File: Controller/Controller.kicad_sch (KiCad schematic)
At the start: 40 parts, among them SW2 SW_Push, SW3 SW_Push, SW4 SW_Push, SW5 SW_Push, SW6 SW_Push, SW7 SW_Push, SW8 SW_Push, SW9 SW_Push

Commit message: Add sections
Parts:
- R1: value ??? -> 400
- renumbered ON/OFF-Switch to ON/OFF-Switch1
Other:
- moved on the sheet: C1, LED1, LED10, LED2, LED3, LED4, LED5, LED6, LED7, LED8, LED9, Level-Shifter-1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

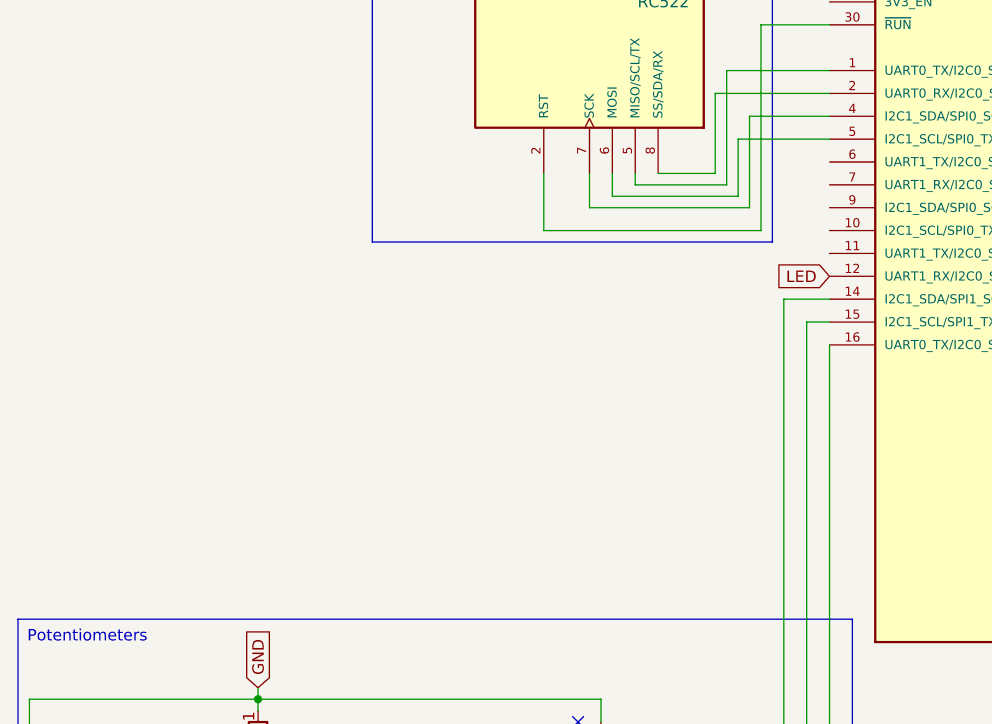
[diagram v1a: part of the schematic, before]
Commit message: Edit symbols and add screen to schematic
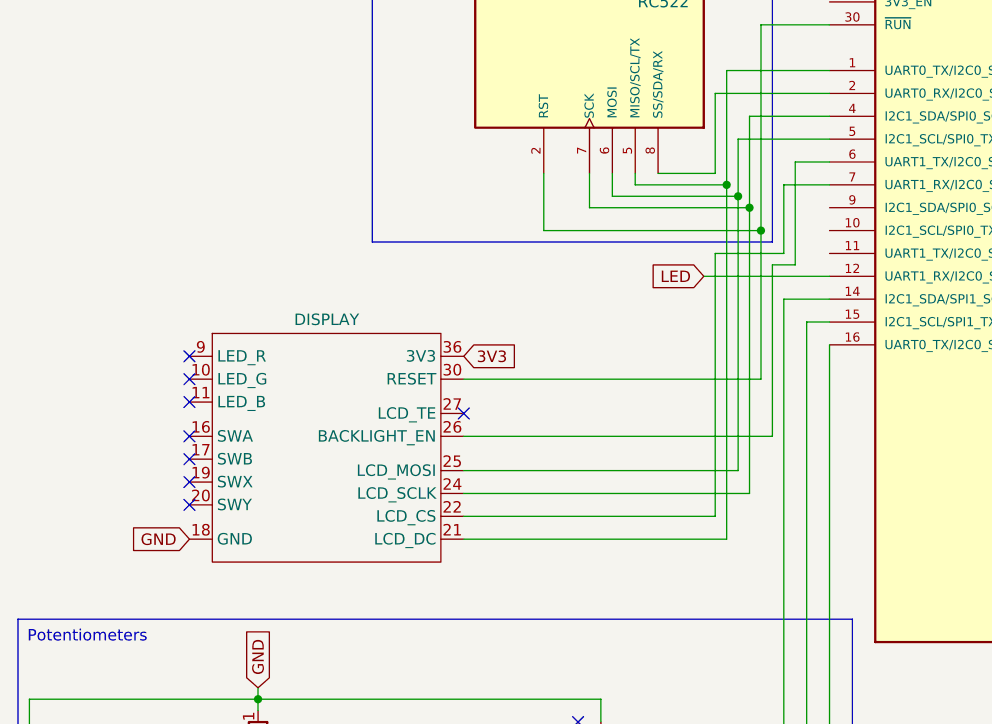
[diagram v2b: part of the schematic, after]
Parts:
- added DISPLAY: ~, symbol PIM580:PIM580
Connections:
- net 3V3: now also DISPLAY.36 (3V3)
- net GND: now also DISPLAY.18 (GND)
- net at NFC-1.5 (MISO/SCL/TX), PICO-1.1 (UART0_TX/I2C0_SDA/SPI0_RX/GP0): now also DISPLAY.21 (LCD_DC)
- net at NFC-1.2 (RST), PICO-1.30 (~{RUN}): now also DISPLAY.30 (RESET)
- net at NFC-1.7 (SCK), PICO-1.4 (I2C1_SDA/SPI0_SCK/GP2): now also DISPLAY.24 (LCD_SCLK)
- net at NFC-1.6 (MOSI), PICO-1.5 (I2C1_SCL/SPI0_TX/GP3): now also DISPLAY.25 (LCD_MOSI)
- net at PICO-1.6 (UART1_TX/I2C0_SDA/SPI0_RX/GP4): now also DISPLAY.26 (BACKLIGHT_EN)
- net at PICO-1.7 (UART1_RX/I2C0_SCL/SPI0_CSN/GP5): now also DISPLAY.22 (LCD_CS)
- no-connect marks 19 -> 27

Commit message: Add mosfet definition
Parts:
- MOS-P1: value ??? -> DMG2305UX-7
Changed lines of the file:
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@@
 		(dnp no)
 		(property "Reference" "MOS-P1"
-			(at 276.352 46.482 90)
+			(at 275.844 50.292 90)
 			(effects
 				(font
@@
 			)
 		)
-		(property "Value" "???"
-			(at 276.352 49.022 90)
+		(property "Value" "DMG2305UX-7"
+			(at 275.844 52.832 90)
 			(effects
 				(font

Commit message: Update
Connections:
- net GP22: now reaches PICO-1.29 (GP22)
- net GP22: now also NFC-1.2 (RST)
- net at DISPLAY.30 (RESET), PICO-1.30 (~{RUN}): no longer NFC-1.2 (RST)
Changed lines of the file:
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@@
-	)
-	(junction
-		(at 95.25 100.33)
-		(diameter 0)
-		(color 0 0 0 0)
 	)
 	(junction
@@
 	(wire
 		(pts
-			(xy 71.12 100.33) (xy 71.12 93.98)
-		)
-		(stroke
-			(width 0)
-			(type default)
-		)
-	)
-	(wire
-		(pts
 			(xy 93.98 87.63) (xy 93.98 97.79)
 		)
@@
 	(wire
 		(pts
-			(xy 95.25 100.33) (xy 95.25 116.84)
+			(xy 95.25 77.47) (xy 95.25 116.84)
 		)
 		(stroke
@@
 	(wire
 		(pts
-			(xy 95.25 77.47) (xy 95.25 100.33)
-		)
-		(stroke
-			(width 0)
-			(type default)
-		)
-	)
-	(wire
-		(pts
 			(xy 76.2 97.79) (xy 76.2 93.98)
 		)
@@
 			(type default)
 			(color 255 0 0 1)
-		)
-	)
-	(wire
-		(pts
-			(xy 95.25 100.33) (xy 71.12 100.33)
-		)
-		(stroke
-			(width 0)
-			(type default)
 		)
 	)
@@
 			)
 			(justify left top)
+		)
+	)
+	(global_label "GP22"
+		(shape input)
+		(at 199.39 105.41 0)
+		(fields_autoplaced yes)
+		(effects
+			(font
+				(size 1.27 1.27)
+			)
+			(justify left)
+		)
+		(property "Intersheetrefs" "${INTERSHEET_REFS}"
+			(at 207.3342 105.41 0)
+			(effects
+				(font
+					(size 1.27 1.27)
+				)
+				(justify left)
+				(hide yes)
+			)
 		)
 	)
@@
 			(effects
 				(font
+					(size 1.27 1.27)
+				)
+				(justify right)
+				(hide yes)
+			)
+		)
+	)
+	(global_label "GP22"
+		(shape input)
+		(at 71.12 93.98 270)
+		(fields_autoplaced yes)
+		(effects
+			(font
+				(size 1.27 1.27)
+			)
+			(justify right)
+		)
+		(property "Intersheetrefs" "${INTERSHEET_REFS}"
+			(at 71.12 101.9242 90)
+			(effects
+				(font

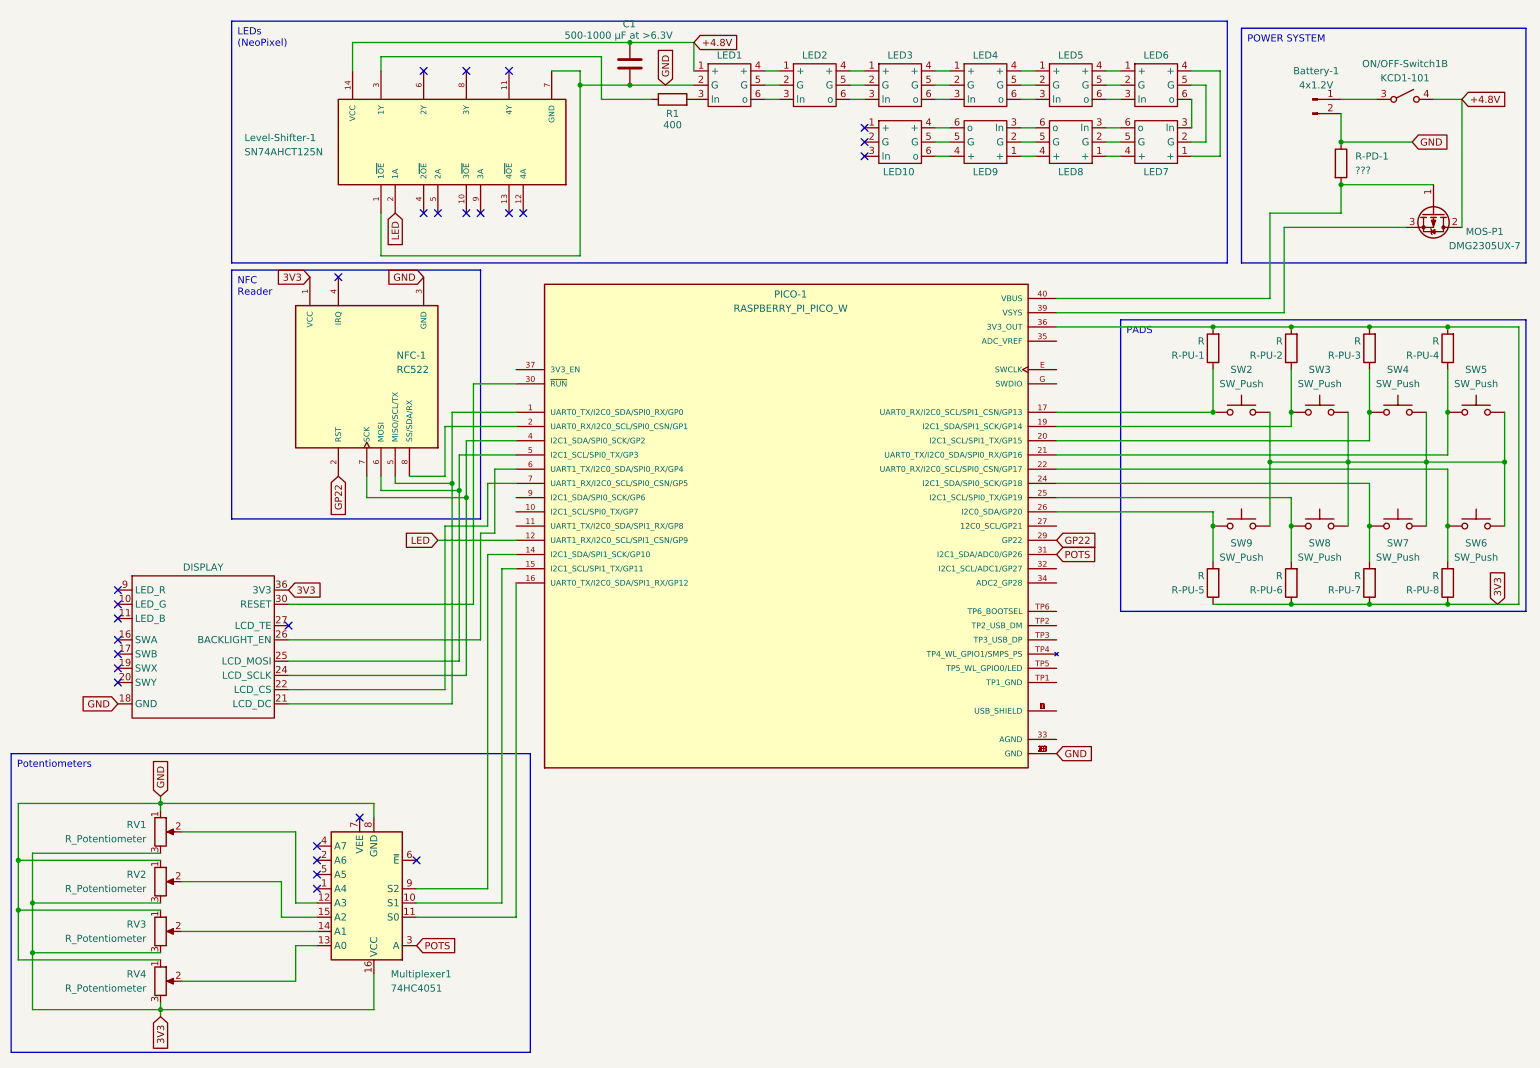
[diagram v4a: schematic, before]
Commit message: Rewire display
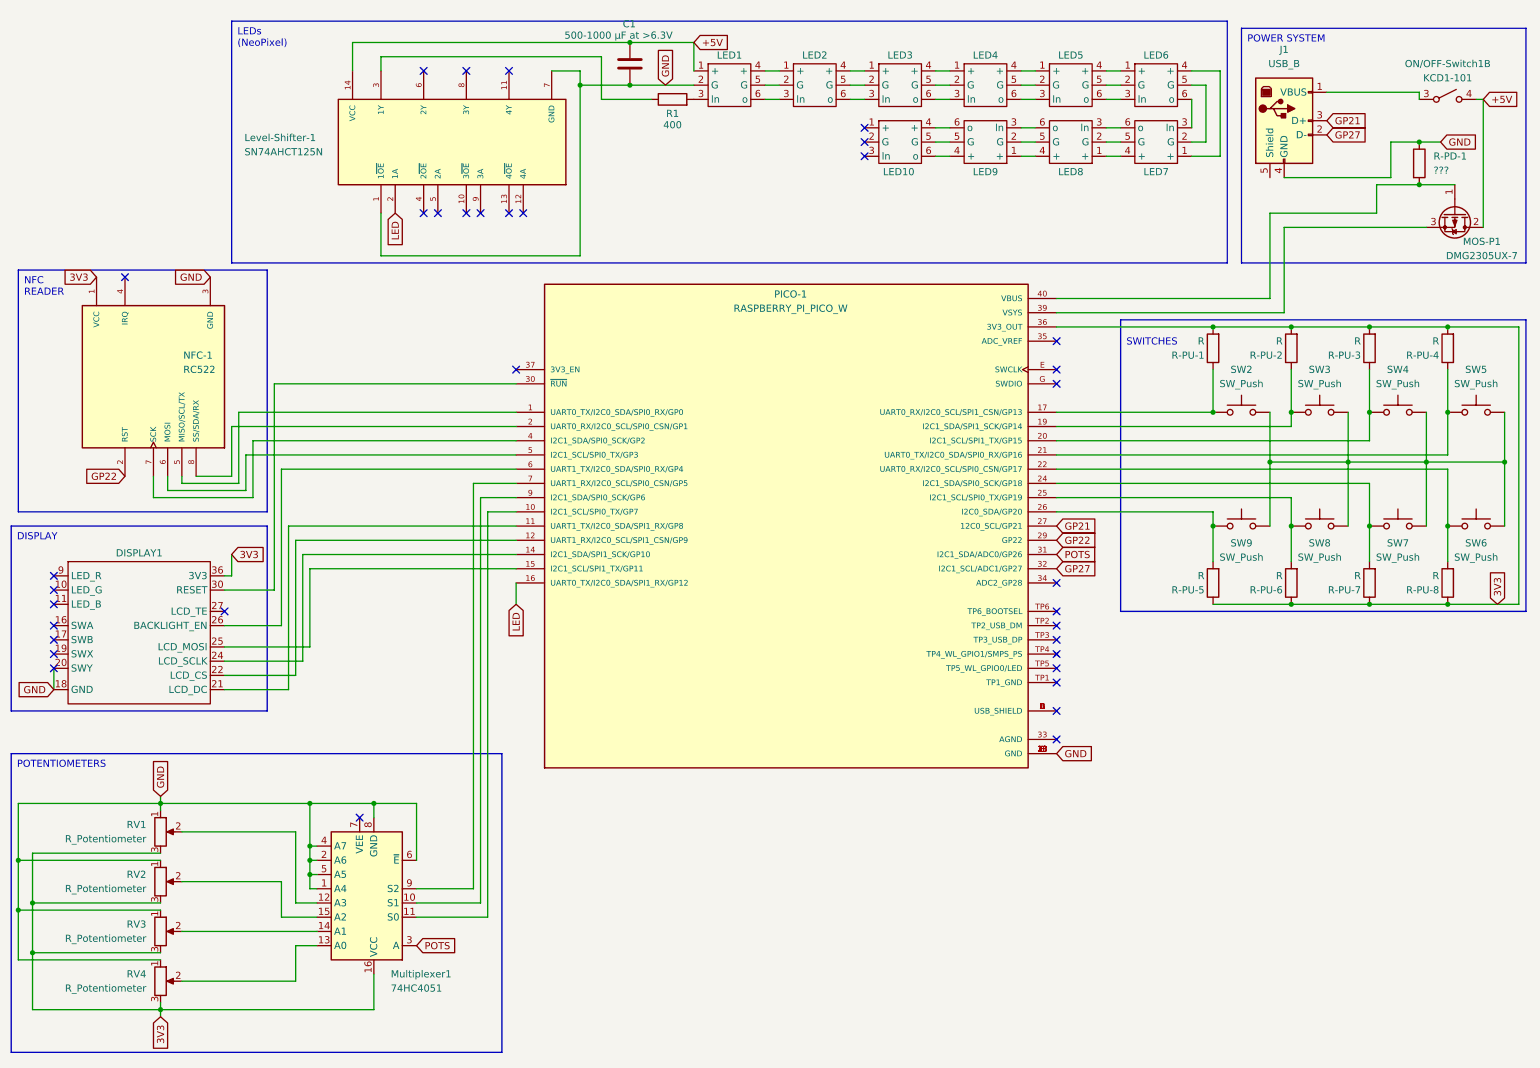
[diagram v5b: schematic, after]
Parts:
- removed Battery-1: 4x1.2V, Connector_PinHeader_1.00mm:PinHeader_1x02_P1.00mm_Vertical, symbol Connector:Conn_01x02_Pin
- added J1: USB_B, Connector_PinHeader_1.00mm:PinHeader_1x04_P1.00mm_Vertical, symbol Connector:USB_B
- DISPLAY1: renamed from DISPLAY; footprint (none) -> Connector_PinHeader_1.00mm:PinHeader_1x08_P1.00mm_Vertical
- MOS-P1: footprint Package_TO_SOT_THT:TO-220-3_Vertical -> (none)
- NFC-1: footprint CEG006900:MODULE_CEG006900 -> Connector_PinHeader_1.00mm:PinHeader_1x07_P1.00mm_Vertical
- R1: footprint (none) -> Resistor_THT:R_Axial_DIN0204_L3.6mm_D1.6mm_P5.08mm_Horizontal
- SW2, SW3, SW4, SW5, SW6, SW7, SW8, SW9: footprint Button_Switch_THT:SW_PUSH-12mm -> (none)
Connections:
- net GND: now also DISPLAY1.20 (SWY), Multiplexer1.1 (A4), Multiplexer1.2 (A6), Multiplexer1.4 (A7), Multiplexer1.5 (A5), Multiplexer1.6 (~{E}), J1.4 (GND)
- net LED: now also PICO-1.16 (UART0_TX/I2C0_SDA/SPI1_RX/GP12); no longer PICO-1.12 (UART1_RX/I2C0_SCL/SPI1_CSN/GP9)
- net at NFC-1.5 (MISO/SCL/TX), PICO-1.1 (UART0_TX/I2C0_SDA/SPI0_RX/GP0): no longer DISPLAY1.21 (LCD_DC)
- net at PICO-1.10 (I2C1_SCL/SPI0_TX/GP7): now also Multiplexer1.11 (S0)
- net at PICO-1.11 (UART1_TX/I2C0_SDA/SPI1_RX/GP8): now also DISPLAY1.21 (LCD_DC)
- net at PICO-1.14 (I2C1_SDA/SPI1_SCK/GP10): now also DISPLAY1.24 (LCD_SCLK); no longer Multiplexer1.9 (S2)
- net at PICO-1.15 (I2C1_SCL/SPI1_TX/GP11): now also DISPLAY1.25 (LCD_MOSI); no longer Multiplexer1.10 (S1)
- net GP21: now reaches PICO-1.27 (12C0_SCL/GP21)
- net GP21: now also J1.3 (D+)
- net GP27: now reaches PICO-1.32 (I2C1_SCL/ADC1/GP27)
- net GP27: now also J1.2 (D-)
- net at NFC-1.7 (SCK), PICO-1.4 (I2C1_SDA/SPI0_SCK/GP2): no longer DISPLAY1.24 (LCD_SCLK)
- net at NFC-1.6 (MOSI), PICO-1.5 (I2C1_SCL/SPI0_TX/GP3): no longer DISPLAY1.25 (LCD_MOSI)
- net at DISPLAY1.22 (LCD_CS): now also PICO-1.12 (UART1_RX/I2C0_SCL/SPI1_CSN/GP9); no longer PICO-1.7 (UART1_RX/I2C0_SCL/SPI0_CSN/GP5)
- net at PICO-1.9 (I2C1_SDA/SPI0_SCK/GP6): now also Multiplexer1.10 (S1)
- net at ON/OFF-Switch1.3 (A): now also J1.1 (VBUS)
- net +4.8V renamed +5V
- new net: Multiplexer1.9 (S2), PICO-1.7 (UART1_RX/I2C0_SCL/SPI0_CSN/GP5)
- no-connect marks 27 -> 35
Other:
- moved on the sheet: DISPLAY1, MOS-P1, NFC-1, ON/OFF-Switch1B, R-PD-1

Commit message: Add components and lign up PCB
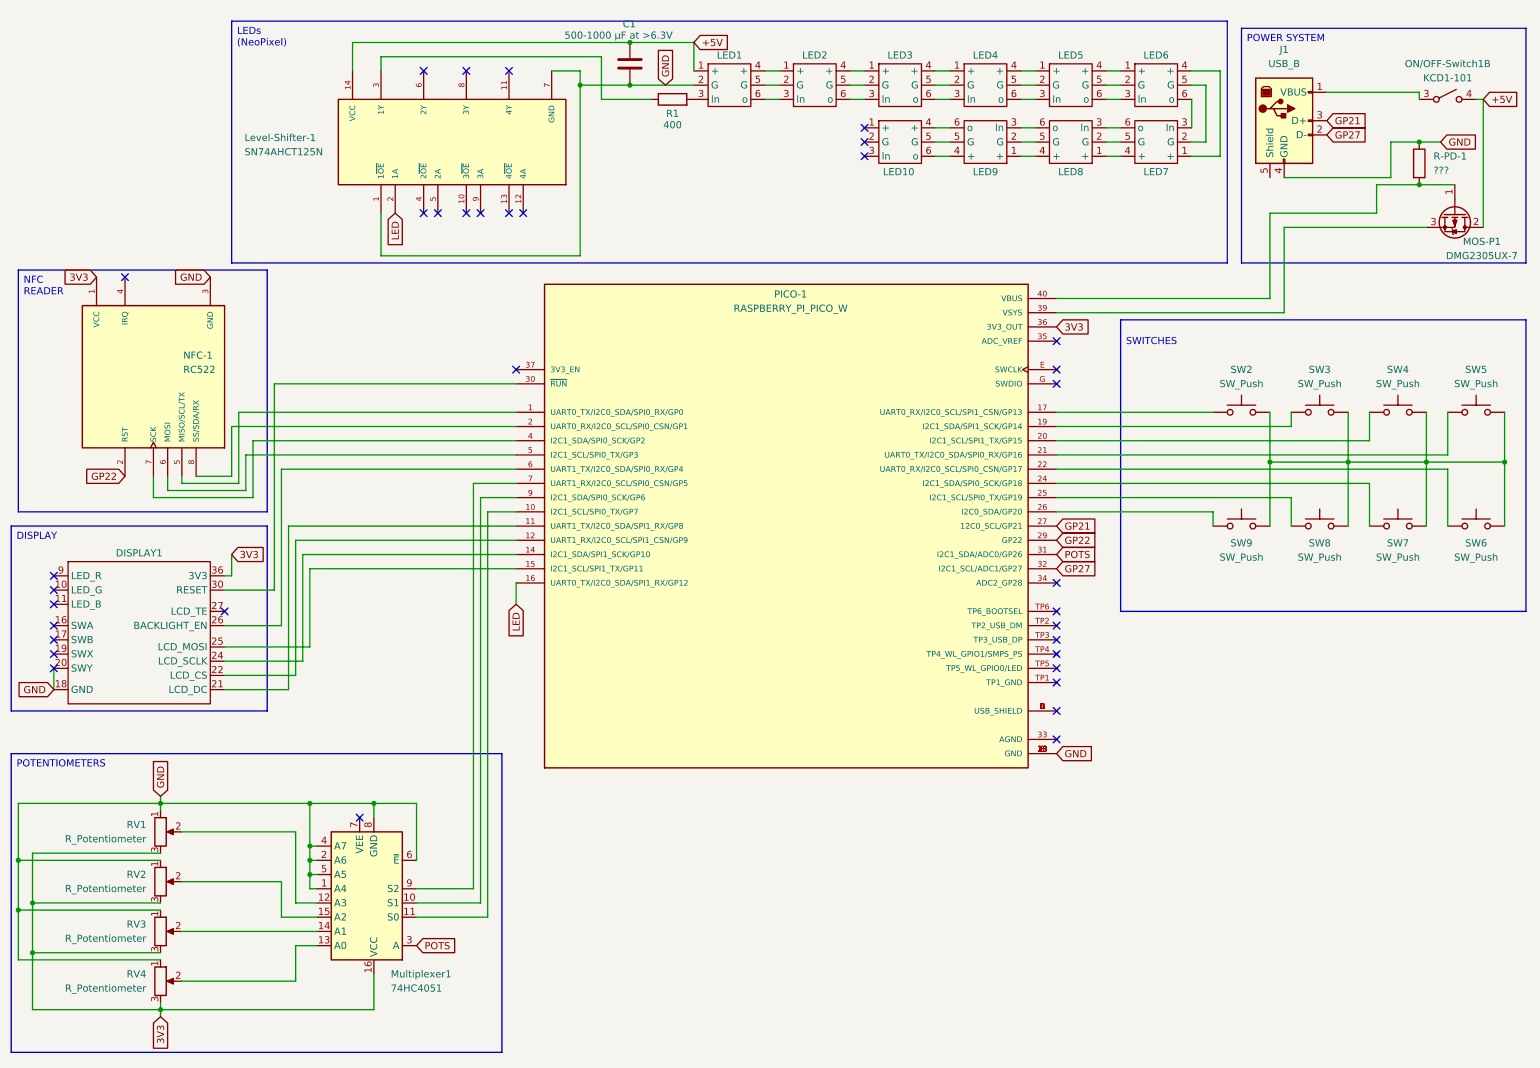
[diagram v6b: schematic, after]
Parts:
- removed R-PU-1, R-PU-2, R-PU-3, R-PU-4, R-PU-5, R-PU-6, R-PU-7, R-PU-8: R, Resistor_THT:R_Axial_DIN0204_L3.6mm_D1.6mm_P5.08mm_Horizontal, symbol Device:R
- DISPLAY1: footprint Connector_PinHeader_1.00mm:PinHeader_1x08_P1.00mm_Vertical -> PIM580:display-footprint
- PICO-1: footprint RASPBERRY_PI_PICO_W:MODULE_RASPBERRY_PI_PICO_W -> RASPBERRY_PI_PICO_W:pico-footprint
- SW2, SW3, SW4, SW5, SW6, SW7, SW8, SW9: footprint (none) -> Gateron:SW_Gateron_LowProfile_HotSwap_THT (1)

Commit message: PCB Routing
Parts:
- removed MOS-P1: DMG2305UX-7, symbol Transistor_FET:FQP27P06
- removed R-PD-1: ???, Resistor_THT:R_Axial_DIN0204_L3.6mm_D1.6mm_P5.08mm_Horizontal, symbol Device:R
- added LDR_R1: ???, Resistor_THT:R_Axial_DIN0204_L3.6mm_D1.6mm_P5.08mm_Horizontal, symbol Device:R
- added R2: LDR03, Connector_PinHeader_1.00mm:PinHeader_1x02_P1.00mm_Vertical, symbol Sensor_Optical:LDR03
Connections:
- net +5V: now also ON/OFF-Switch1.2 (B), PICO-1.39 (VSYS); no longer ON/OFF-Switch1.4 (B)
- net 3V3: now also R2.2
- net GND: now also LDR_R1.1; no longer Multiplexer1.1 (A4)
- net at J1.1 (VBUS): now also ON/OFF-Switch1.1 (A); no longer ON/OFF-Switch1.3 (A)
- new net: LDR_R1.2, Multiplexer1.1 (A4), R2.1
- no-connect marks 35 -> 37
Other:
- moved on the sheet: ON/OFF-Switch1A

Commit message: Update PCB
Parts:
- J1: footprint Connector_PinHeader_1.00mm:PinHeader_1x04_P1.00mm_Vertical -> Connector_PinHeader_2.54mm:PinHeader_1x04_P2.54mm_Vertical
- NFC-1: footprint Connector_PinHeader_1.00mm:PinHeader_1x07_P1.00mm_Vertical -> Connector_PinHeader_2.54mm:PinHeader_1x07_P2.54mm_Vertical
- ON/OFF-Switch1, R2: footprint Connector_PinHeader_1.00mm:PinHeader_1x02_P1.00mm_Vertical -> Connector_PinHeader_2.54mm:PinHeader_1x02_P2.54mm_Vertical
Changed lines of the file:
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@@
 			)
 		)
-		(property "Footprint" "Connector_PinHeader_1.00mm:PinHeader_1x07_P1.00mm_Vertical"
+		(property "Footprint" "Connector_PinHeader_2.54mm:PinHeader_1x07_P2.54mm_Vertical"
 			(at 38.1 76.2 0)
 			(effects
@@
 			)
 		)
-		(property "Footprint" "Connector_PinHeader_1.00mm:PinHeader_1x02_P1.00mm_Vertical"
+		(property "Footprint" "Connector_PinHeader_2.54mm:PinHeader_1x02_P2.54mm_Vertical"
 			(at 269.24 25.4 0)
 			(effects
@@
 			)
 		)
-		(property "Footprint" "Connector_PinHeader_1.00mm:PinHeader_1x04_P1.00mm_Vertical"
+		(property "Footprint" "Connector_PinHeader_2.54mm:PinHeader_1x04_P2.54mm_Vertical"
 			(at 243.84 31.75 0)
 			(effects
@@
 			)
 		)
-		(property "Footprint" "Connector_PinHeader_1.00mm:PinHeader_1x02_P1.00mm_Vertical"
+		(property "Footprint" "Connector_PinHeader_2.54mm:PinHeader_1x02_P2.54mm_Vertical"
 			(at 61.595 163.83 90)
 			(effects
